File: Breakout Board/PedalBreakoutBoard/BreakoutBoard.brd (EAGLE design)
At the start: 68.2 x 58.4 mm, 40 parts

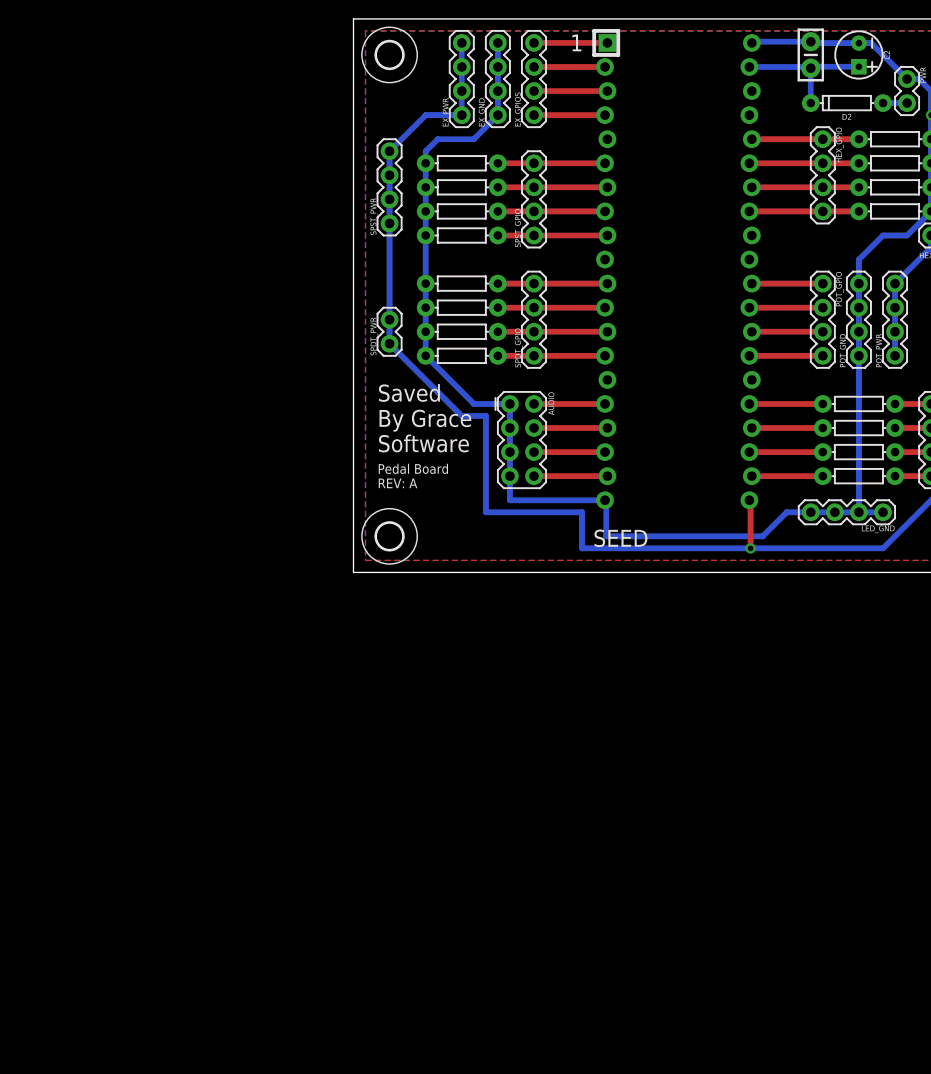
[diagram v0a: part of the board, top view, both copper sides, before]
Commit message: DP-33 - Added power section
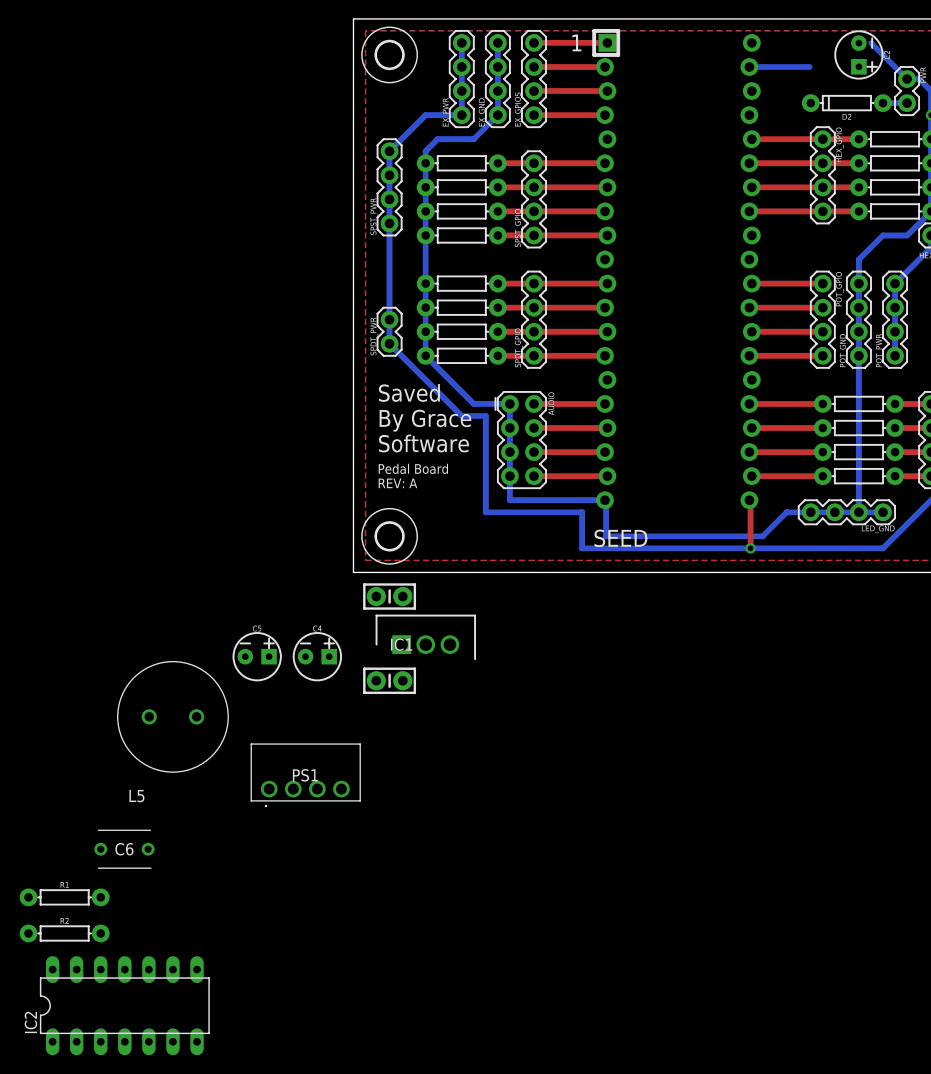
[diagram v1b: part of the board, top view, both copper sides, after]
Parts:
- added C3: 0.1uF, SparkFun-Capacitors:CAP-PTH-SMALL-KIT
- added C4, C5: 10uF, SparkFun-Capacitors:CPOL-RADIAL-2.5MM-5MM
- added C6: RDEC71H226MWK1H03B, SamacSys_Parts:RCEC71H226MWK1H03B
- added IC1: LD1117V, SamacSys_Parts:TO255P460X1020X2008-3P
- added IC2: MCP604P, linear:DIL14
- added L5: 7447471022, SamacSys_Parts:WE-TIS_111190
- added PS1: RFM-0505S, SamacSys_Parts:RFM0505S
- added R1, R2: 100k, SparkFun-Resistors:AXIAL-0.3
- moved C1 79.6 mm to (3.81, -11.4), turned to 0 degrees
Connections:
- new net +5V_ISOL: C6.1, PS1.4, R1.P$2
- new net N$6: R1.P$1, R2.P$2
- new net N$7: C5.1, L5.2, PS1.2
- new net N$8: C4.1, IC1.2, L5.1
- new net V+: IC2.4
- new net V-: IC2.11
- net +9V_IN: now also C3.1, IC1.3
- net GND: now also C3.2, C4.2, C5.2, C6.2, IC1.1, PS1.1, PS1.3, R2.P$1
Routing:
- net GND: track 173.9 -> 161.4 mm
- net +9V_IN: track 15.4 -> 6.35 mm

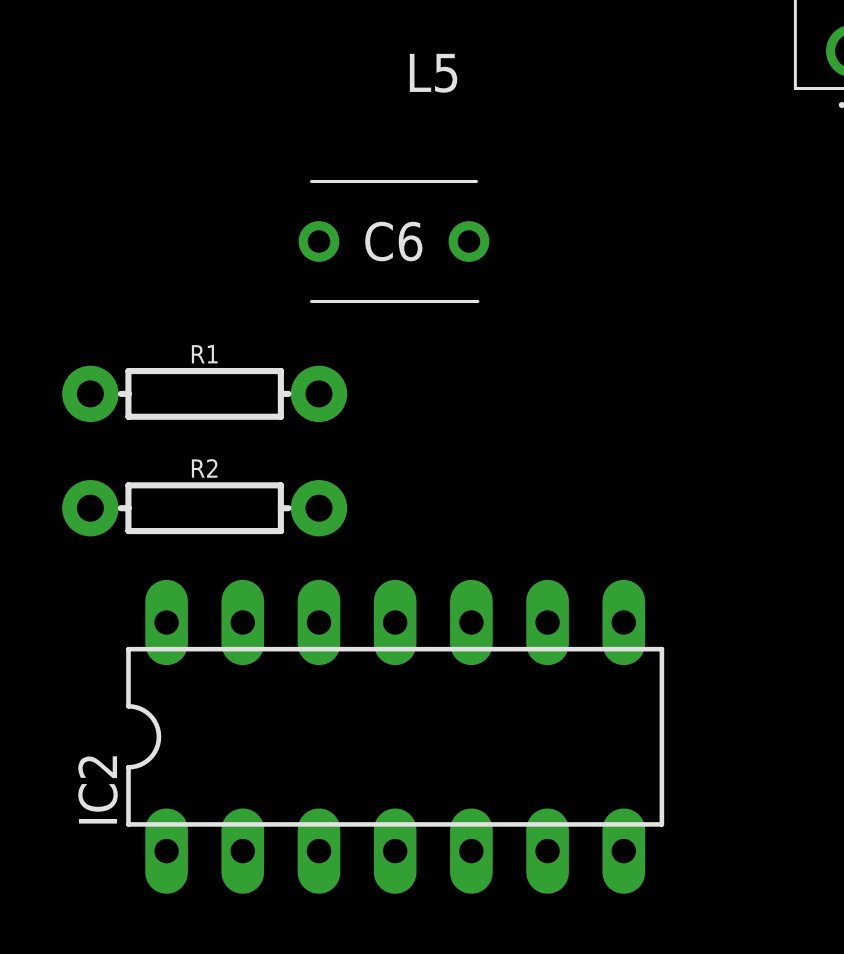
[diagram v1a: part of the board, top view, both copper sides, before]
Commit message: DP-33 - Add custom library and 22uf capacitor
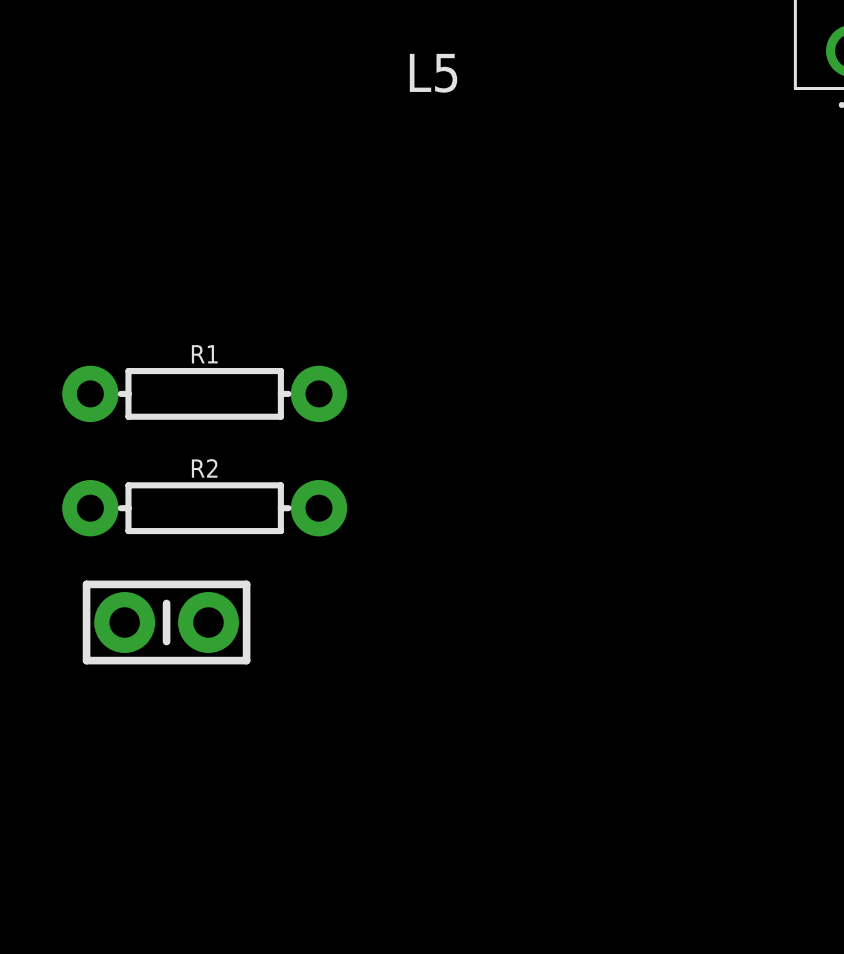
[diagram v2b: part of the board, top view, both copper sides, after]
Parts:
- removed IC2: MCP604P, linear:DIL14
- C6: value RDEC71H226MWK1H03B -> 22UF; device SamacSys_Parts:RCEC71H226MWK1H03B -> Custom-Parts:CAP-PTH-SMALL-KIT
- moved C6 13.7 mm to (-31.8, -41.9)
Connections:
- removed net V+: IC2.4
- removed net V-: IC2.11
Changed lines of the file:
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@@
 <attribute name="VALUE" x="-22.86" y="-8.795" size="1.27" layer="27" align="center"/>
-</element>
-<element name="C6" library="SamacSys_Parts" package="RCEC71H226MWK1H03B" value="RDEC71H226MWK1H03B" x="-26.67" y="-29.21" smashed="yes">
-<attribute name="DESCRIPTION" value="Capacitor L=5.5mm W=7.5mm T=4.0mm" x="-26.67" y="-29.21" size="1.778" layer="27" display="off"/>
-<attribute name="HEIGHT" value="10mm" x="-26.67" y="-29.21" size="1.778" layer="27" display="off"/>
-<attribute name="MANUFACTURER_NAME" value="Murata Electronics" x="-26.67" y="-29.21" size="1.778" layer="27" display="off"/>
-<attribute name="MANUFACTURER_PART_NUMBER" value="RDEC71H226MWK1H03B" x="-26.67" y="-29.21" size="1.778" layer="27" display="off"/>
-<attribute name="MOUSER_PART_NUMBER" value="81-RDEC71H226MWK1H3B" x="-26.67" y="-29.21" size="1.778" layer="27" display="off"/>
-<attribute name="MOUSER_PRICE-STOCK" value="https://www.mouser.co.uk/ProductDetail/Murata-Electronics/RDEC71H226MWK1H03B?qs=QzBtWTOodeV2kUwqUMKnLA%3D%3D" x="-26.67" y="-29.21" size="1.778" layer="27" display="off"/>
-<attribute name="NAME" x="-24.17" y="-29.21" size="1.27" layer="25" align="center"/>
-<attribute name="VALUE" x="-24.17" y="-29.21" size="1.27" layer="27" align="center"/>
 </element>
 <element name="R1" library="SparkFun-Resistors" library_urn="urn:adsk.eagle:library:532" package="AXIAL-0.3" package3d_urn="urn:adsk.eagle:package:39658/1" value="100k" x="-30.48" y="-34.29" smashed="yes">
@@
 <attribute name="VALUE" x="-30.48" y="-39.116" size="0.6096" layer="27" font="vector" ratio="20" align="top-center"/>
 </element>
-<element name="IC2" library="linear" library_urn="urn:adsk.eagle:library:262" package="DIL14" package3d_urn="urn:adsk.eagle:package:16407/2" value="MCP604P" x="-24.13" y="-45.72" smashed="yes">
-<attribute name="NAME" x="-33.401" y="-48.768" size="1.27" layer="25" ratio="10" rot="R90"/>
-<attribute name="POPULARITY" value="0" x="-24.13" y="-45.72" size="1.778" layer="27" display="off"/>
-<attribute name="VALUE" x="-30.861" y="-46.355" size="1.27" layer="27" ratio="10"/>
-</element>
+<element name="C6" library="Custom-Parts" package="CAP-PTH-SMALL-KIT" value="22UF" x="-31.75" y="-41.91" smashed="yes"/>
 </elements>
 <signals>
@@
 <contactref element="PS1" pad="1"/>
 <contactref element="PS1" pad="3"/>
+<contactref element="R2" pad="P$1"/>
 <contactref element="C6" pad="2"/>
-<contactref element="R2" pad="P$1"/>
 <wire x1="54.63" y1="55.86" x2="53.34" y2="55.86" width="0" layer="19" extent="16-16"/>
 <wire x1="42.164" y1="56.007" x2="53.34" y2="55.86" width="0" layer="19" extent="16-16"/>
@@
 <wire x1="-3.81" y1="-22.86" x2="-5.06" y2="-8.89" width="0" layer="19" extent="1-1"/>
 <wire x1="-8.89" y1="-22.86" x2="-3.81" y2="-22.86" width="0" layer="19" extent="1-1"/>
-<wire x1="-21.67" y1="-29.21" x2="-8.89" y2="-22.86" width="0" layer="19" extent="1-1"/>
-<wire x1="-34.29" y1="-38.1" x2="-21.67" y2="-29.21" width="0" layer="19" extent="1-1"/>
+<wire x1="-30.353" y1="-41.91" x2="-8.89" y2="-22.86" width="0" layer="19" extent="1-1"/>
+<wire x1="-34.29" y1="-38.1" x2="-30.353" y2="-41.91" width="0" layer="19" extent="1-1"/>
 </signal>
 <signal name="SPST1">
@@
 <signal name="+5V_ISOL">
 <contactref element="PS1" pad="4"/>
+<contactref element="R1" pad="P$2"/>
 <contactref element="C6" pad="1"/>
-<contactref element="R1" pad="P$2"/>
-<wire x1="-26.67" y1="-29.21" x2="-26.67" y2="-34.29" width="0" layer="19" extent="1-1"/>
-<wire x1="-1.27" y1="-22.86" x2="-26.67" y2="-29.21" width="0" layer="19" extent="1-1"/>
+<wire x1="-26.67" y1="-34.29" x2="-33.147" y2="-41.91" width="0" layer="19" extent="1-1"/>
+<wire x1="-1.27" y1="-22.86" x2="-26.67" y2="-34.29" width="0" layer="19" extent="1-1"/>
 </signal>
 <signal name="N$6">
@@
 <wire x1="-26.67" y1="-38.1" x2="-34.29" y2="-34.29" width="0" layer="19" extent="1-1"/>
 </signal>
-<signal name="V+">
-<contactref element="IC2" pad="4"/>
-</signal>
-<signal name="V-">
-<contactref element="IC2" pad="11"/>
-</signal>
 </signals>

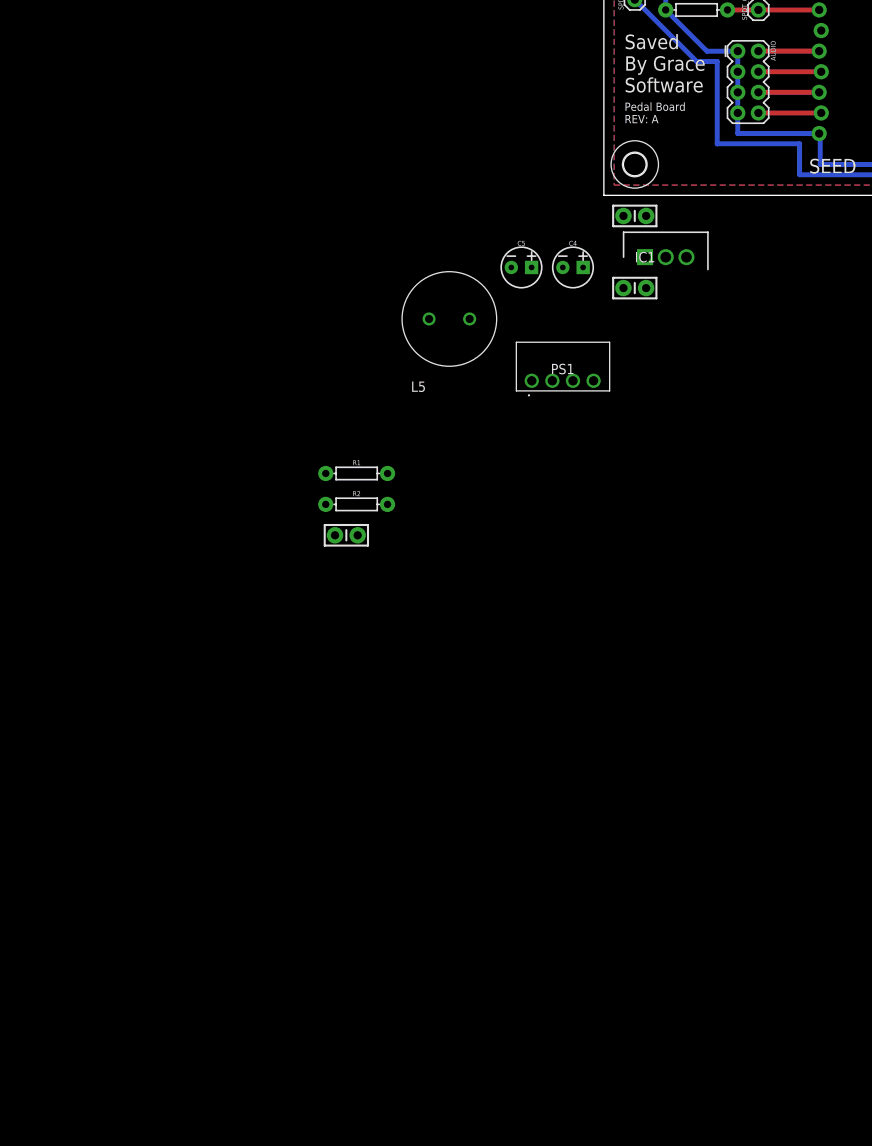
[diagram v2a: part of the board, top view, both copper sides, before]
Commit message: DP-33 - Add remaining audio noise schematic
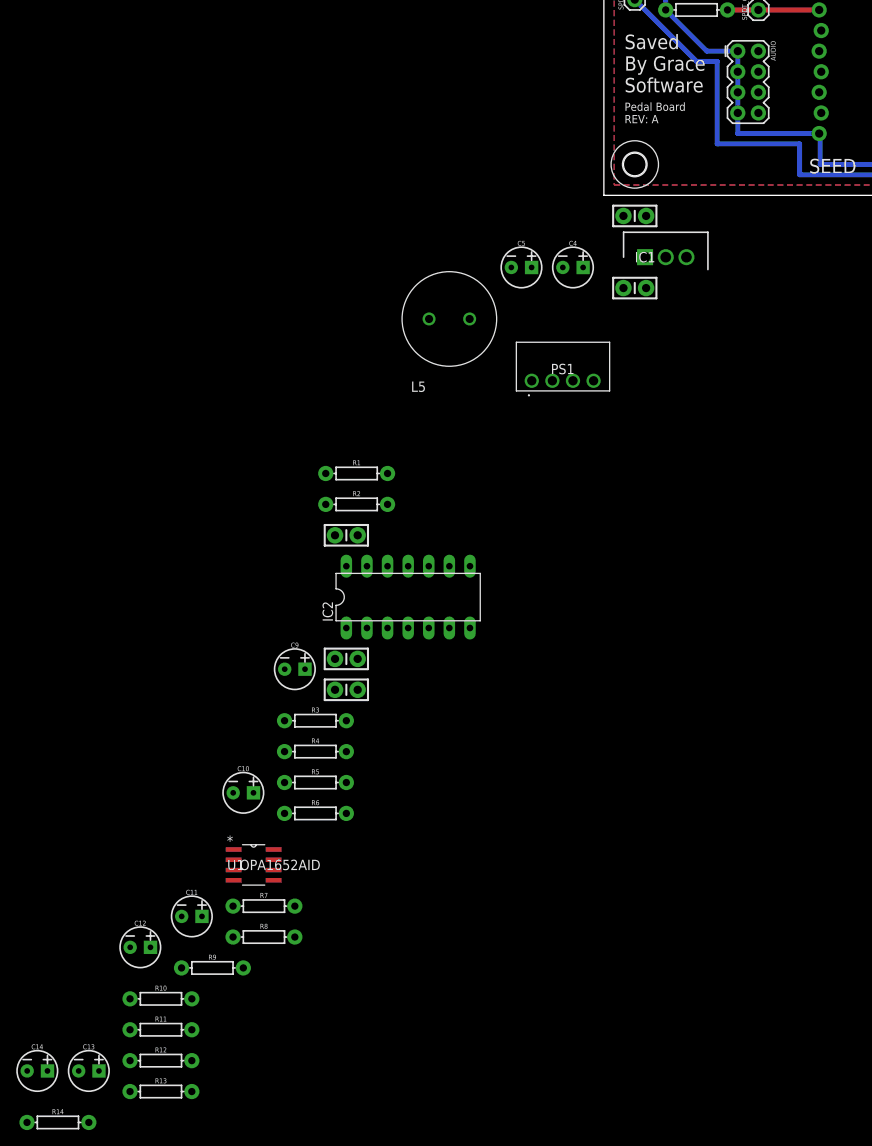
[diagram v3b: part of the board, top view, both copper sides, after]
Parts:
- added C10, C11, C12, C13, C14, C9: 10uF, SparkFun-Capacitors:CPOL-RADIAL-2.5MM-5MM
- added C7, C8: 0.1uF, SparkFun-Capacitors:CAP-PTH-SMALL-KIT
- added IC2: MCP6004P, Custom-Parts:DIL14
- added R10, R11, R12, R13, R14, R3, R4, R5, R6, R7, R8: 2M, Custom-Parts:AXIAL-0.3
- added R9: 100, SparkFun-Resistors:AXIAL-0.3
- added U1: OPA1652AID, Custom-Parts:D8
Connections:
- new net IN_L_JACK: AUDIO.2, C9.2, R4.P$2
- new net IN_R_JACK: AUDIO.4, C10.2, R6.P$2
- new net N$10: IC2.13, IC2.14
- new net N$11: C10.1, IC2.5, R5.P$1
- new net N$12: C11.2, R7.P$1, R8.P$2, U1.3
- new net N$13: R9.P$1, U1.1, U1.2
- new net N$14: C12.1, R9.P$2
- new net N$15: C13.2, R11.P$1, R12.P$2, U1.5
- new net N$16: C14.1, R13.P$2
- new net N$17: R13.P$1, U1.6, U1.7
- new net N$9: C9.1, IC2.10, R3.P$1
- new net OUT_L_JACK: AUDIO.6, C12.2, R10.P$2
- new net OUT_R_JACK: AUDIO.8, C14.2, R14.P$1
- new net V_AUDIOBIAS: IC2.1, IC2.2, R3.P$2, R5.P$2
- net +5V_ISOL: now also C7.1, C8.1, IC2.4, R11.P$2, R7.P$2, U1.8
- net GND: now also C7.2, C8.2, IC2.11, IC2.12, R10.P$1, R12.P$1, R14.P$2, R4.P$1, R6.P$1, R8.P$1, U1.4
- net IN_L: now also IC2.8, IC2.9; no longer AUDIO.2
- net IN_R: now also IC2.6, IC2.7; no longer AUDIO.4
- net N$6: now also IC2.3
- net OUT_L: now also C11.1; no longer AUDIO.6
- net OUT_R: now also C13.1; no longer AUDIO.8
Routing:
- net OUT_R: track 7.75 -> 0.00 mm
- net IN_R: track 7.75 -> 0.00 mm
- net OUT_L: track 7.49 -> 0.00 mm
- net IN_L: track 7.49 -> 0.00 mm

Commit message: DP-33 - Update breakout board with ceramic capacitors
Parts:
- removed C14: 10uF, SparkFun-Capacitors:CPOL-RADIAL-2.5MM-5MM
- removed D11, D12, D21, D22, H1, H2, H3, H4, S1, S2, S3, S4: 10k, SparkFun-Resistors:AXIAL-0.3
- added C15: 10UF, Custom-Parts:CAP-PTH-SMALL-KIT
- added R15, R16, R17, R18, R19, R20, R21, R22, R23, R24, R25, R26: 10k, SparkFun-Resistors:AXIAL-0.3
- C10, C11, C12, C13, C2, C4, C5, C9: value 10uF -> 10UF; device SparkFun-Capacitors:CPOL-RADIAL-2.5MM-5MM -> Custom-Parts:CAP-PTH-SMALL-KIT
- moved C2 237.0 mm to (-68.6, -148.6), turned to 0 degrees
- moved C4 150.5 mm to (-68.6, -144.8)
- moved C5 144.4 mm to (-68.6, -141.0)
- moved C9 70.4 mm to (-68.6, -121.9)
- moved C10 57.4 mm to (-68.6, -125.7)
- moved C11 44.4 mm to (-68.6, -129.5)
- moved C12 42.2 mm to (-68.6, -133.3)
- moved C13 29.6 mm to (-68.6, -137.2)
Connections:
- net +9V_IN: now also C2.2; no longer C2.1
- net GND: now also C2.1, C4.1, C5.1, R15.P$1, R16.P$1, R17.P$1, R18.P$1, R19.P$1, R20.P$1, R21.P$1, R22.P$1, R23.P$1, R24.P$1, R25.P$1, R26.P$1; no longer C2.2, C4.2, C5.2, D11.P$1, D12.P$1, D21.P$1, D22.P$1, H1.P$1, H2.P$1, H3.P$1, H4.P$1, S1.P$1, S2.P$1, S3.P$1, S4.P$1
- net HEX_1: now also R23.P$2; no longer H1.P$2
- net HEX_2: now also R24.P$2; no longer H2.P$2
- net HEX_3: now also R25.P$2; no longer H3.P$2
- net HEX_4: now also R26.P$2; no longer H4.P$2
- net IN_L_JACK: now also C9.1; no longer C9.2
- net IN_R_JACK: now also C15.1; no longer C10.2
- net N$11: now also C15.2; no longer C10.1
- net N$14: now also C10.1; no longer C12.1
- net N$15: now also C13.1; no longer C13.2
- net N$16: now also C12.2; no longer C14.1
- net N$7: now also C5.2; no longer C5.1
- net N$8: now also C4.2; no longer C4.1
- net N$9: now also C9.2; no longer C9.1
- net OUT_L_JACK: now also C10.2; no longer C12.2
- net OUT_R: now also C13.2; no longer C13.1
- net OUT_R_JACK: now also C12.1; no longer C14.2
- net SPDT1_1: now also R22.P$2; no longer D11.P$2
- net SPDT1_2: now also R21.P$2; no longer D12.P$2
- net SPDT2_1: now also R20.P$2; no longer D21.P$2
- net SPDT2_2: now also R19.P$2; no longer D22.P$2
- net SPST1: now also R18.P$2; no longer S1.P$2
- net SPST2: now also R17.P$2; no longer S2.P$2
- net SPST3: now also R16.P$2; no longer S3.P$2
- net SPST4: now also R15.P$2; no longer S4.P$2
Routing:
- net GND: track 161.4 -> 118.9 mm
- net HEX_4: track 11.6 -> 7.75 mm
- net HEX_3: track 11.3 -> 7.49 mm
- net HEX_2: track 11.6 -> 7.75 mm
- net HEX_1: track 11.3 -> 7.49 mm
- net SPST4: track 11.6 -> 7.75 mm
- net SPST3: track 11.3 -> 7.49 mm
- net SPST2: track 11.6 -> 7.75 mm
- net SPST1: track 11.3 -> 7.49 mm
- net SPDT2_2: track 11.3 -> 7.49 mm
- net SPDT2_1: track 11.6 -> 7.75 mm
- net SPDT1_2: track 11.3 -> 7.49 mm
- net SPDT1_1: track 11.6 -> 7.75 mm
